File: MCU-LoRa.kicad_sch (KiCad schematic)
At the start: 14 parts, among them J1 Conn_01x01_Socket, J2 Conn_01x01_Socket, J3 Conn_01x01_Socket, J4 Conn_01x01_Socket, J5 Conn_01x01_Socket, J6 Conn_01x01_Socket, J7 Conn_01x01_Socket, J8 Conn_01x01_Socket

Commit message: 3v3 trace moved to back side.
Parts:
- J3, J5, J6, J7, J8: symbol Connector:Conn_01x01_Socket -> ProjectLib:Conn_01x01_Socket
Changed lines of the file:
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@@
 	)
 	(symbol
-		(lib_id "Connector:Conn_01x01_Socket")
+		(lib_id "ProjectLib:Conn_01x01_Socket")
 		(at 163.83 109.22 0)
 		(mirror y)
@@
 	)
 	(symbol
-		(lib_id "Connector:Conn_01x01_Socket")
+		(lib_id "ProjectLib:Conn_01x01_Socket")
 		(at 143.51 72.39 0)
 		(mirror y)
@@
 	)
 	(symbol
-		(lib_id "Connector:Conn_01x01_Socket")
+		(lib_id "ProjectLib:Conn_01x01_Socket")
 		(at 67.31 106.68 0)
 		(mirror y)
@@
 	)
 	(symbol
-		(lib_id "Connector:Conn_01x01_Socket")
+		(lib_id "ProjectLib:Conn_01x01_Socket")
 		(at 138.43 68.58 0)
 		(mirror y)
@@
 	)
 	(symbol
-		(lib_id "Connector:Conn_01x01_Socket")
+		(lib_id "ProjectLib:Conn_01x01_Socket")
 		(at 163.83 105.41 0)
 		(mirror y)

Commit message: ongoing
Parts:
- removed J1, J2, J3, J4, J5, J6, J7, J8: Conn_01x01_Socket, ProjectLib:PinSocket_1x01_P2.54mm_Vertical, symbol ProjectLib:Conn_01x01_Socket
- added J7, J8: Conn_01x08_Pin, ProjectLib:castellated_1x08_P2.54mm, symbol ProjectLib:Conn_01x08_Pin
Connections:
- net +3V3: now also J7.2 (Pin_2), J8.1 (Pin_1)
- net GND: now also J7.1 (Pin_1), J8.2 (Pin_2)
- net PA9: now also J8.8 (Pin_8)
- net SCL1: now also J8.4 (Pin_4)
- net SCL2: now also J7.3 (Pin_3)
- net SDA1: now also J8.3 (Pin_3)
- net SDA2: now also J8.7 (Pin_7)
- net VBAT: now also J8.5 (Pin_5)
- no-connect marks 0 -> 6
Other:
- moved on the sheet: C1, C2, C3, C4, R1, R2

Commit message: ongoing cleanup. DRC clean excluding edge cut of castellated holes.
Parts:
- J7, J8: value Conn_01x08_Pin -> castellated_1x08_P2.54
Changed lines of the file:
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@@
 			)
 		)
-		(property "Value" "Conn_01x08_Pin"
+		(property "Value" "castellated_1x08_P2.54"
 			(at 38.862 173.228 0)
 			(effects
@@
 			)
 		)
-		(property "Value" "Conn_01x08_Pin"
+		(property "Value" "castellated_1x08_P2.54"
 			(at 150.876 169.926 0)
 			(effects

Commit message: ongoing
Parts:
- J7, J8: value castellated_1x08_P2.54 -> Conn_01x12_Pin; footprint ProjectLib:castellated_1x08_P2.54mm -> ProjectLib:Castellated_Header_1x12_P2.00mm_Vertical; symbol ProjectLib:Conn_01x08_Pin -> ProjectLib:Conn_01x12_Pin
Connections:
- net +3V3: now also J8.11 (Pin_11), J8.2 (Pin_2); no longer J8.1 (Pin_1)
- net GND: now also J8.1 (Pin_1), J8.12 (Pin_12); no longer J8.2 (Pin_2)
- net PA9: now also J8.4 (Pin_4); no longer J8.8 (Pin_8)
- net SCL1: now also J8.8 (Pin_8); no longer J8.4 (Pin_4)
- net SCL2: now also J7.11 (Pin_11); no longer J7.3 (Pin_3)
- net SDA1: now also J8.9 (Pin_9); no longer J8.3 (Pin_3)
- net SDA2: now also J7.12 (Pin_12); no longer J8.7 (Pin_7)
- net VBAT: now also J8.10 (Pin_10); no longer J8.5 (Pin_5)
- net SWCLK: now reaches J8.6 (Pin_6)
- new net PA8-MCO: J8.3 (Pin_3)
- new net SWDIO: J8.5 (Pin_5)
- no-connect marks 6 -> 0

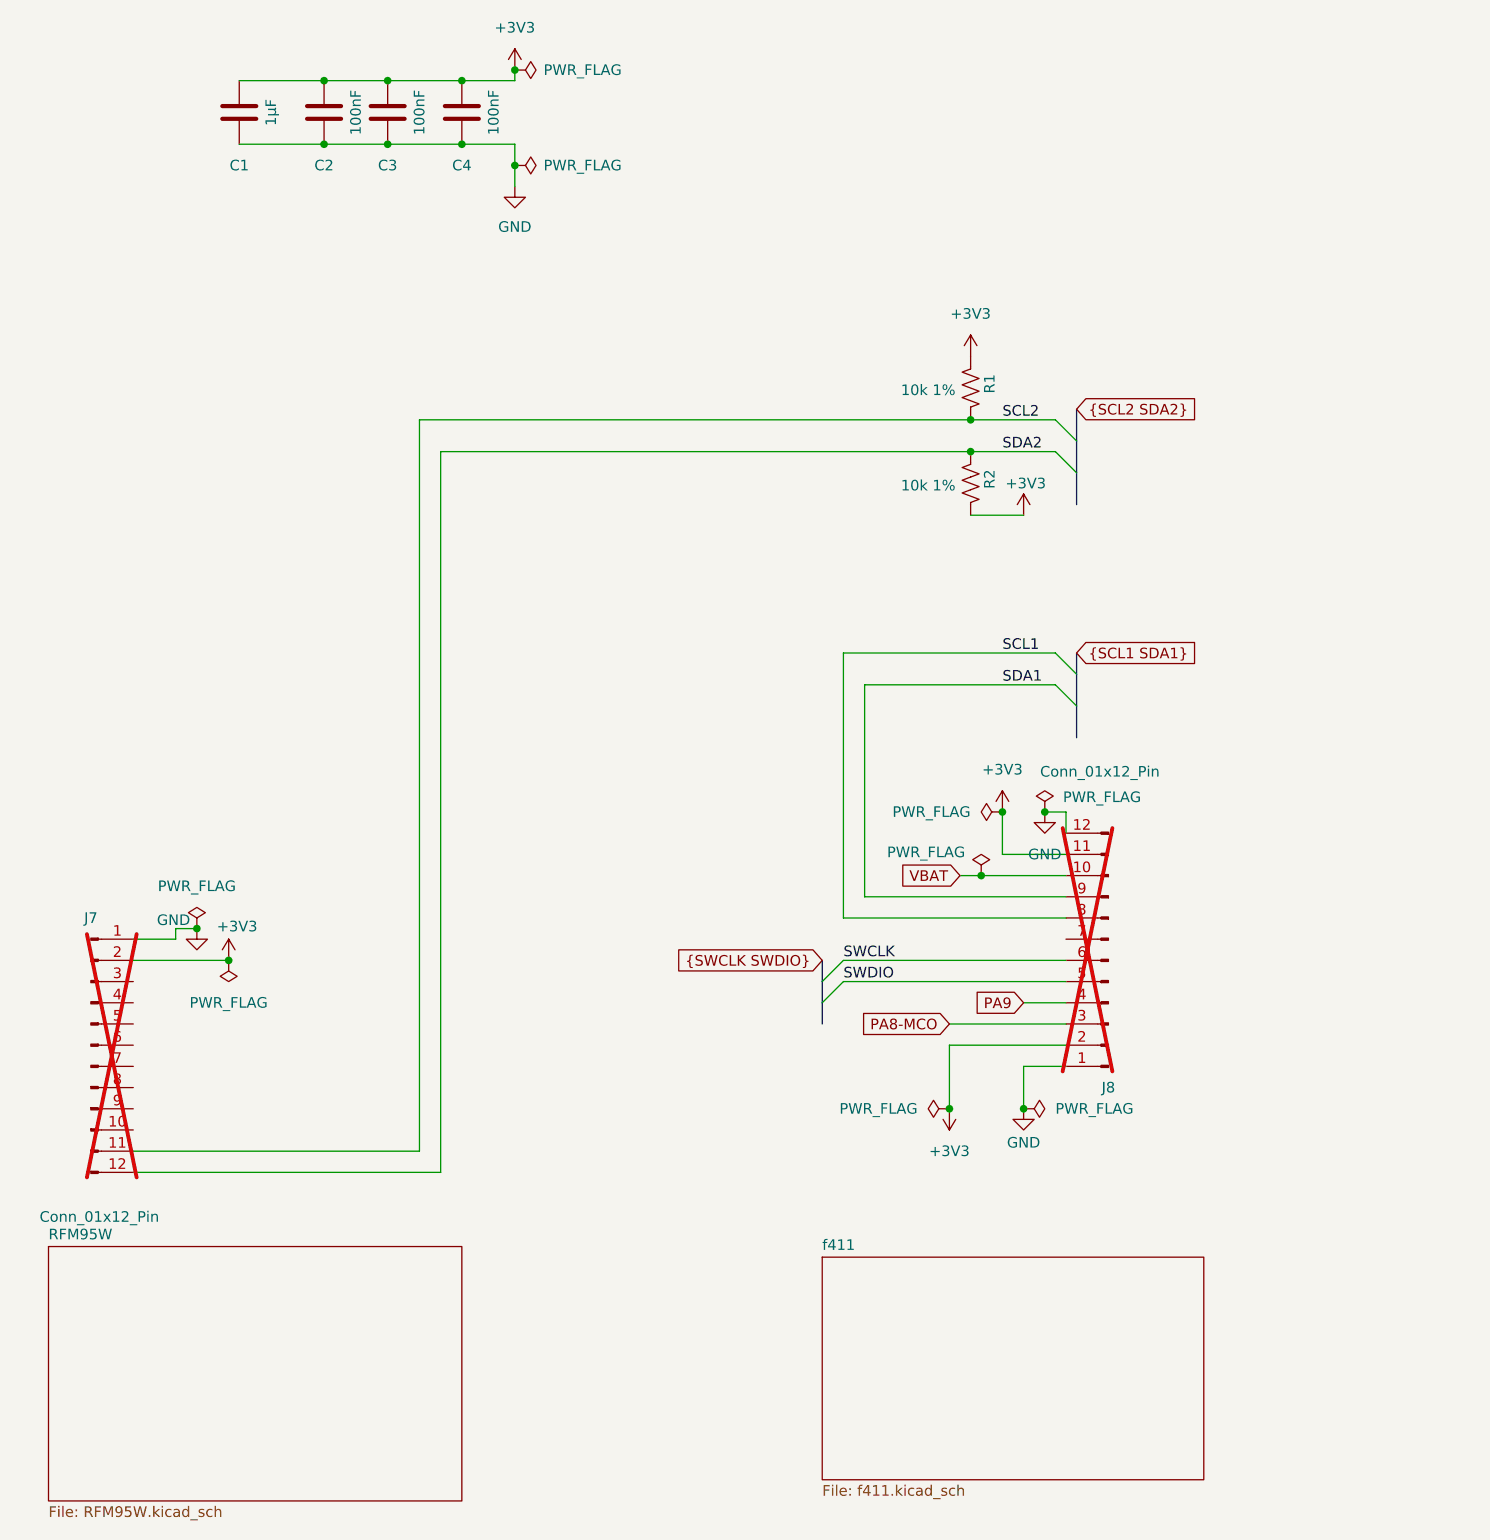
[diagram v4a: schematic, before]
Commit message: settled on 24-pins. Fairly clean castillated pin header but no footprint yet. Decided against rotating radio.
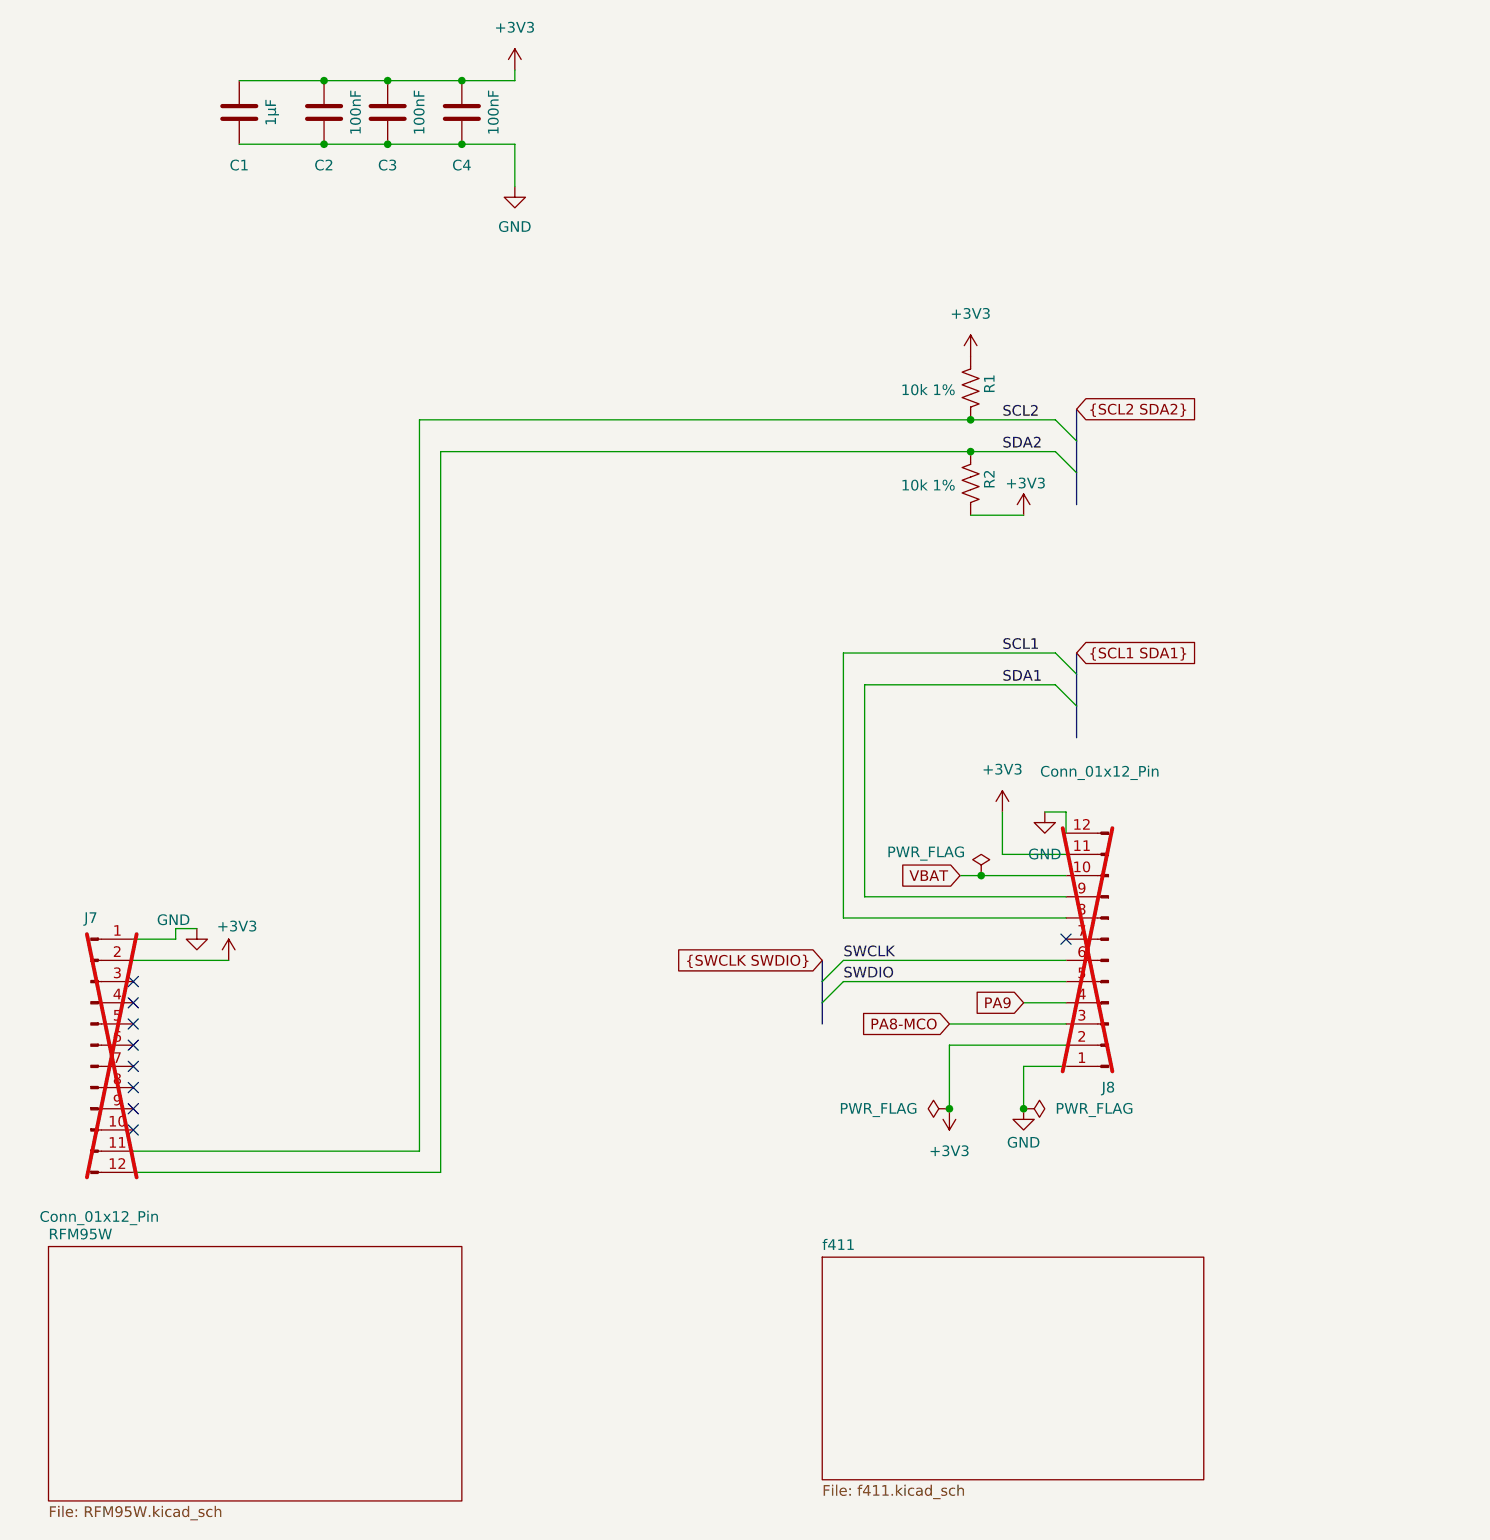
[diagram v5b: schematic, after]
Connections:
- no-connect marks 0 -> 9

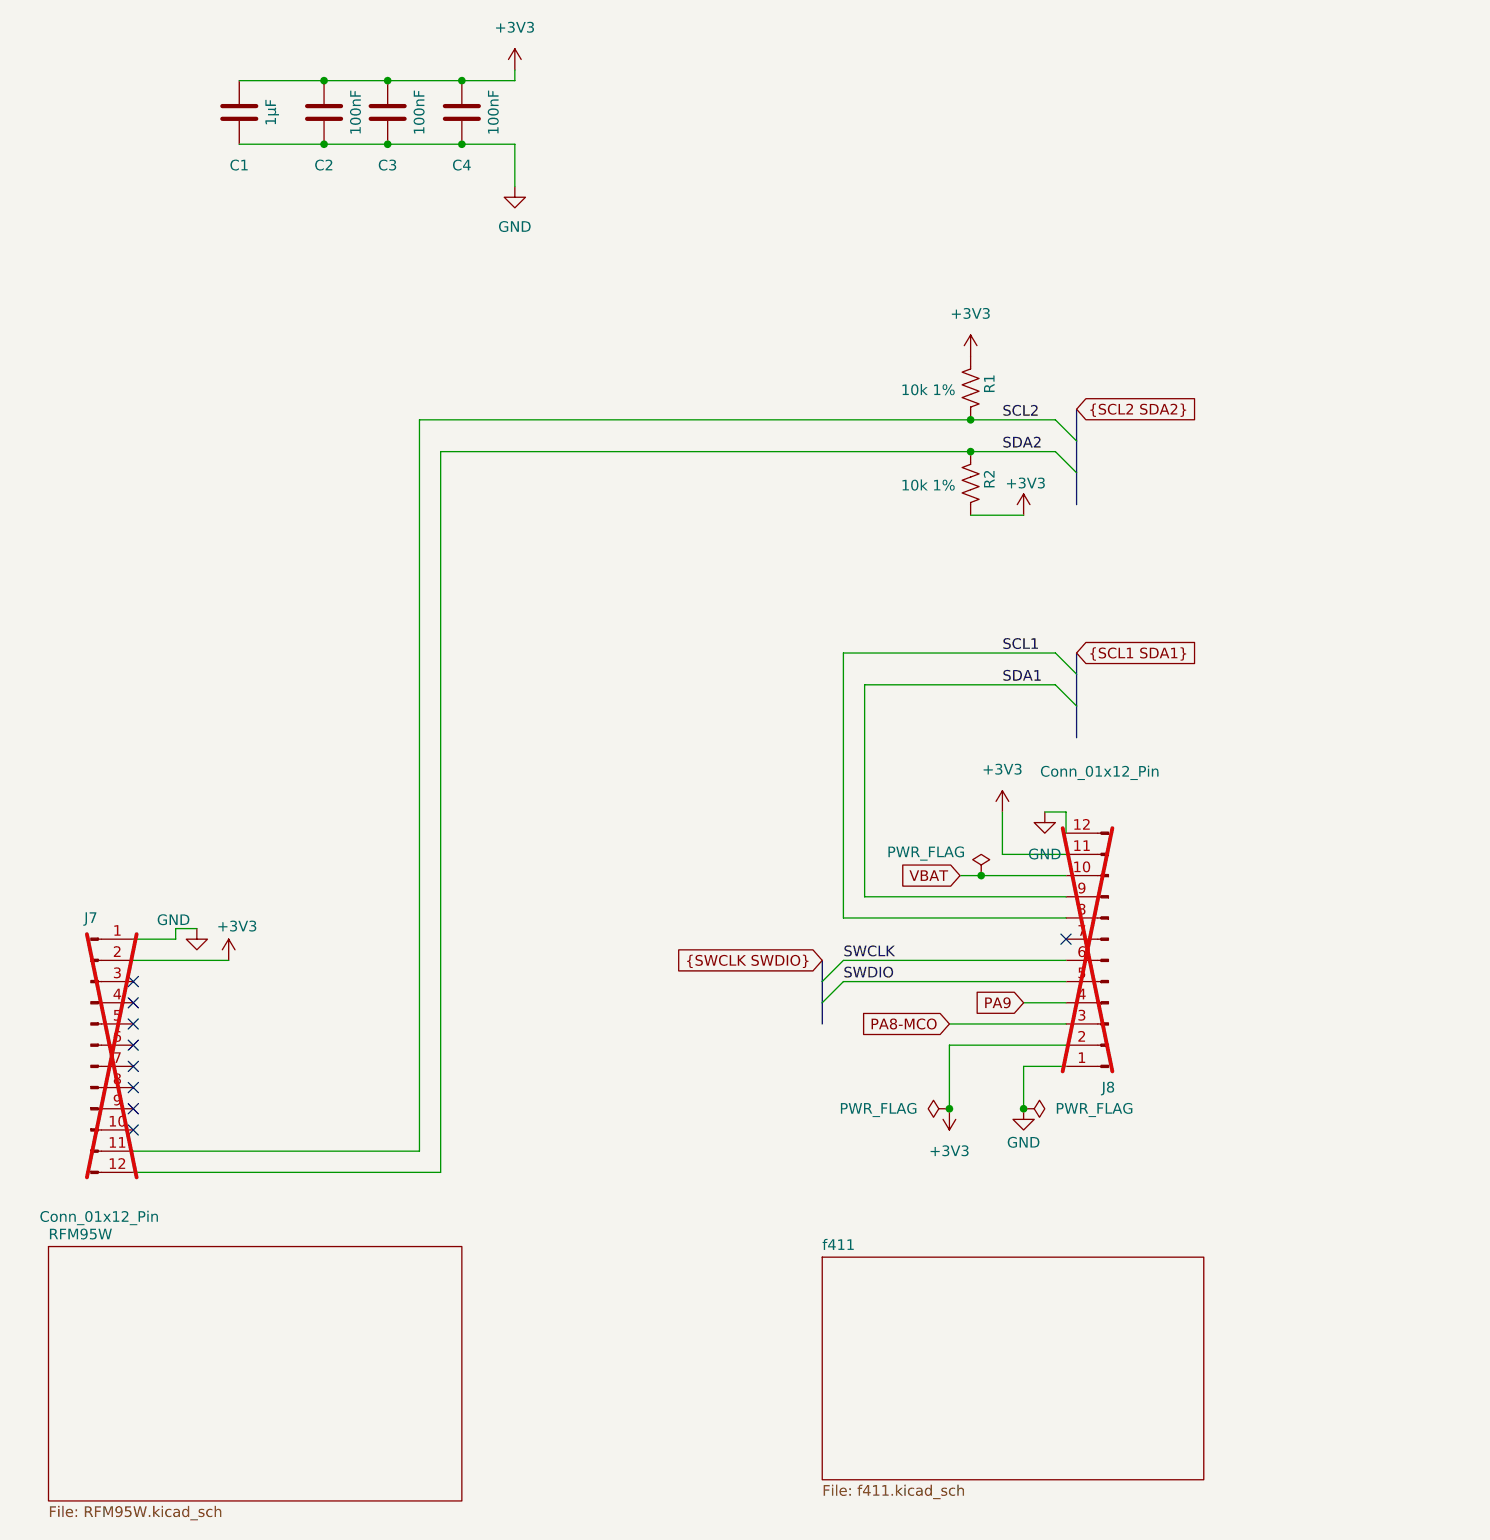
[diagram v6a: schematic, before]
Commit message: added footprint and step model. Cleaned up silkscreen and fab layers.
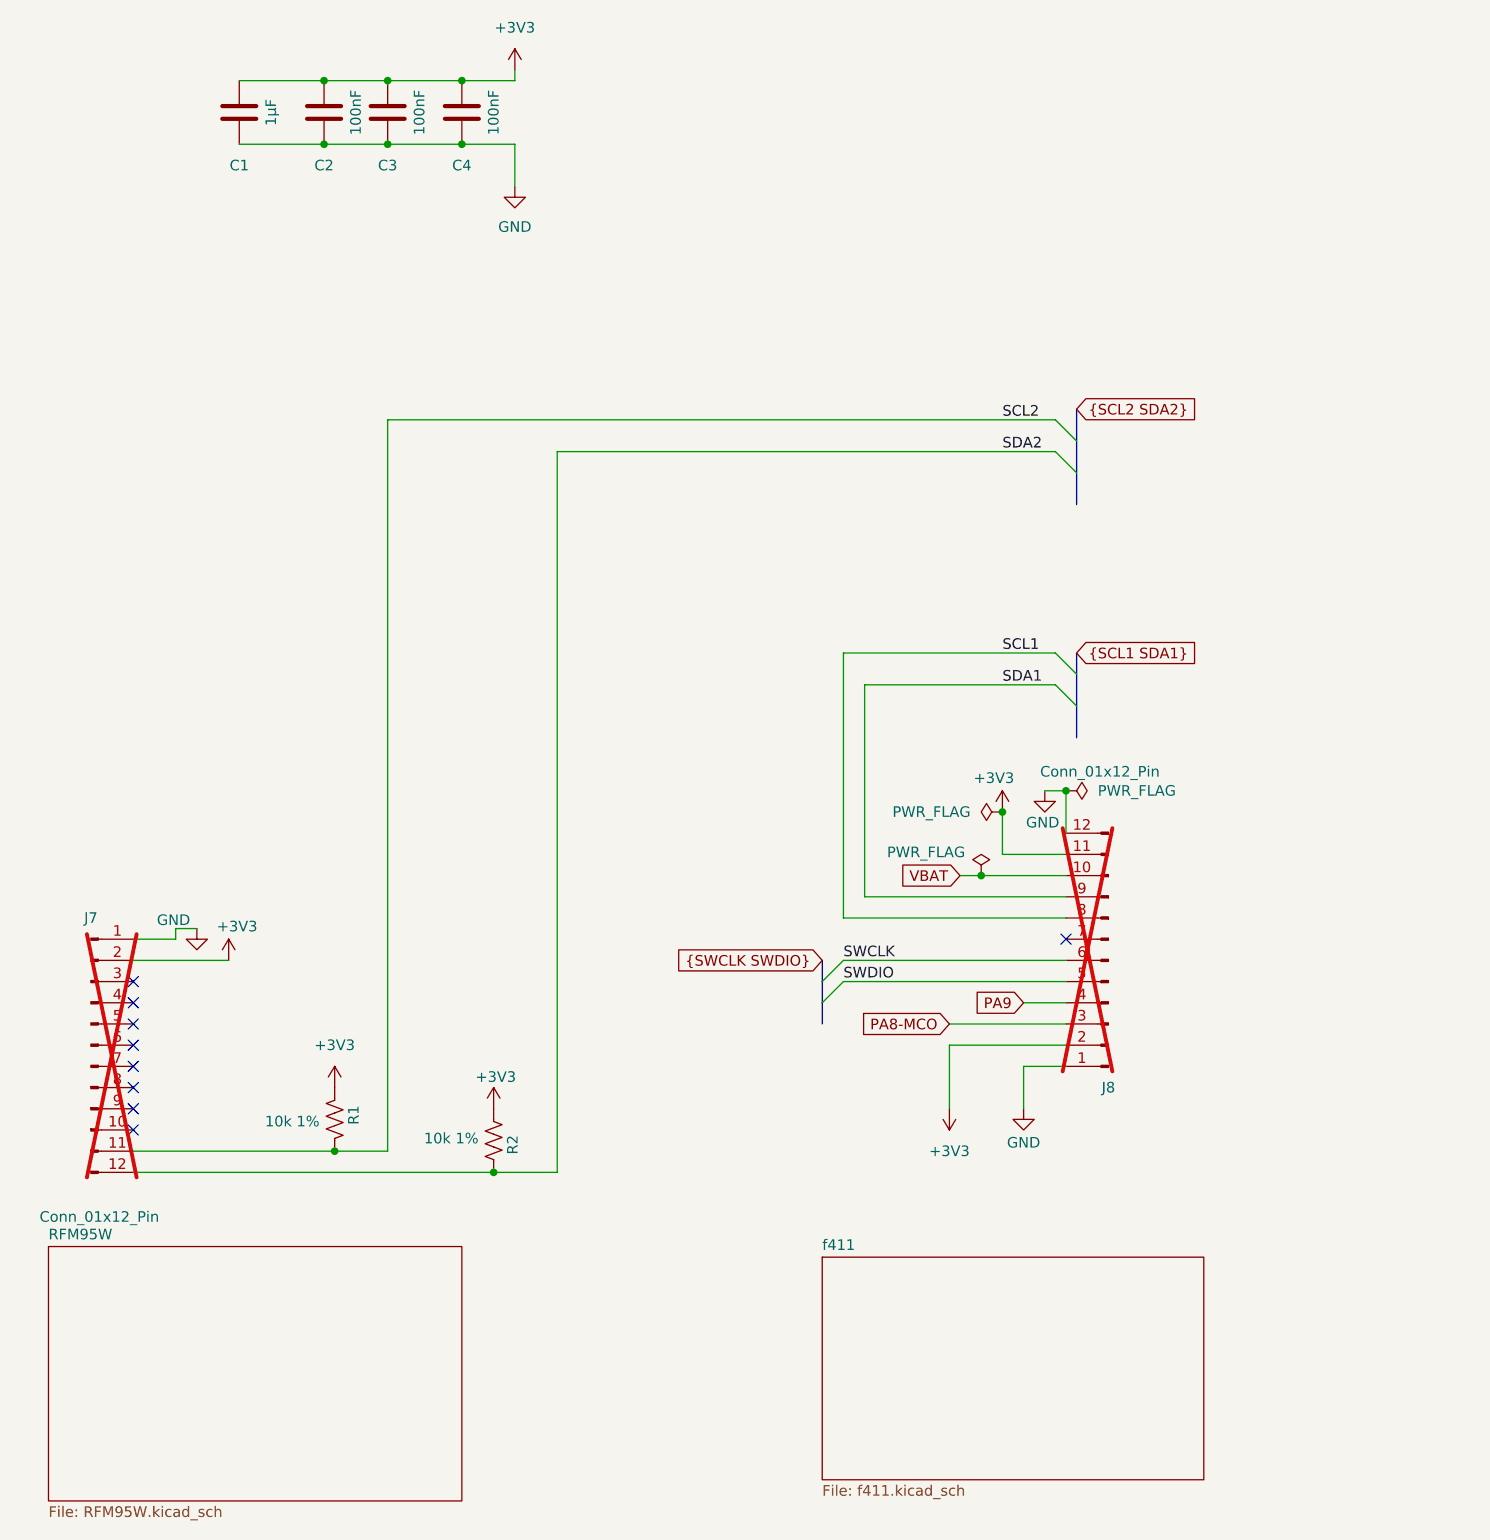
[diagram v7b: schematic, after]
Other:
- moved on the sheet: R1, R2
